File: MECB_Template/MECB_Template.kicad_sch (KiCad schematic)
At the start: 6 parts, among them J1 MECB_64AC, U1 ATF16V8

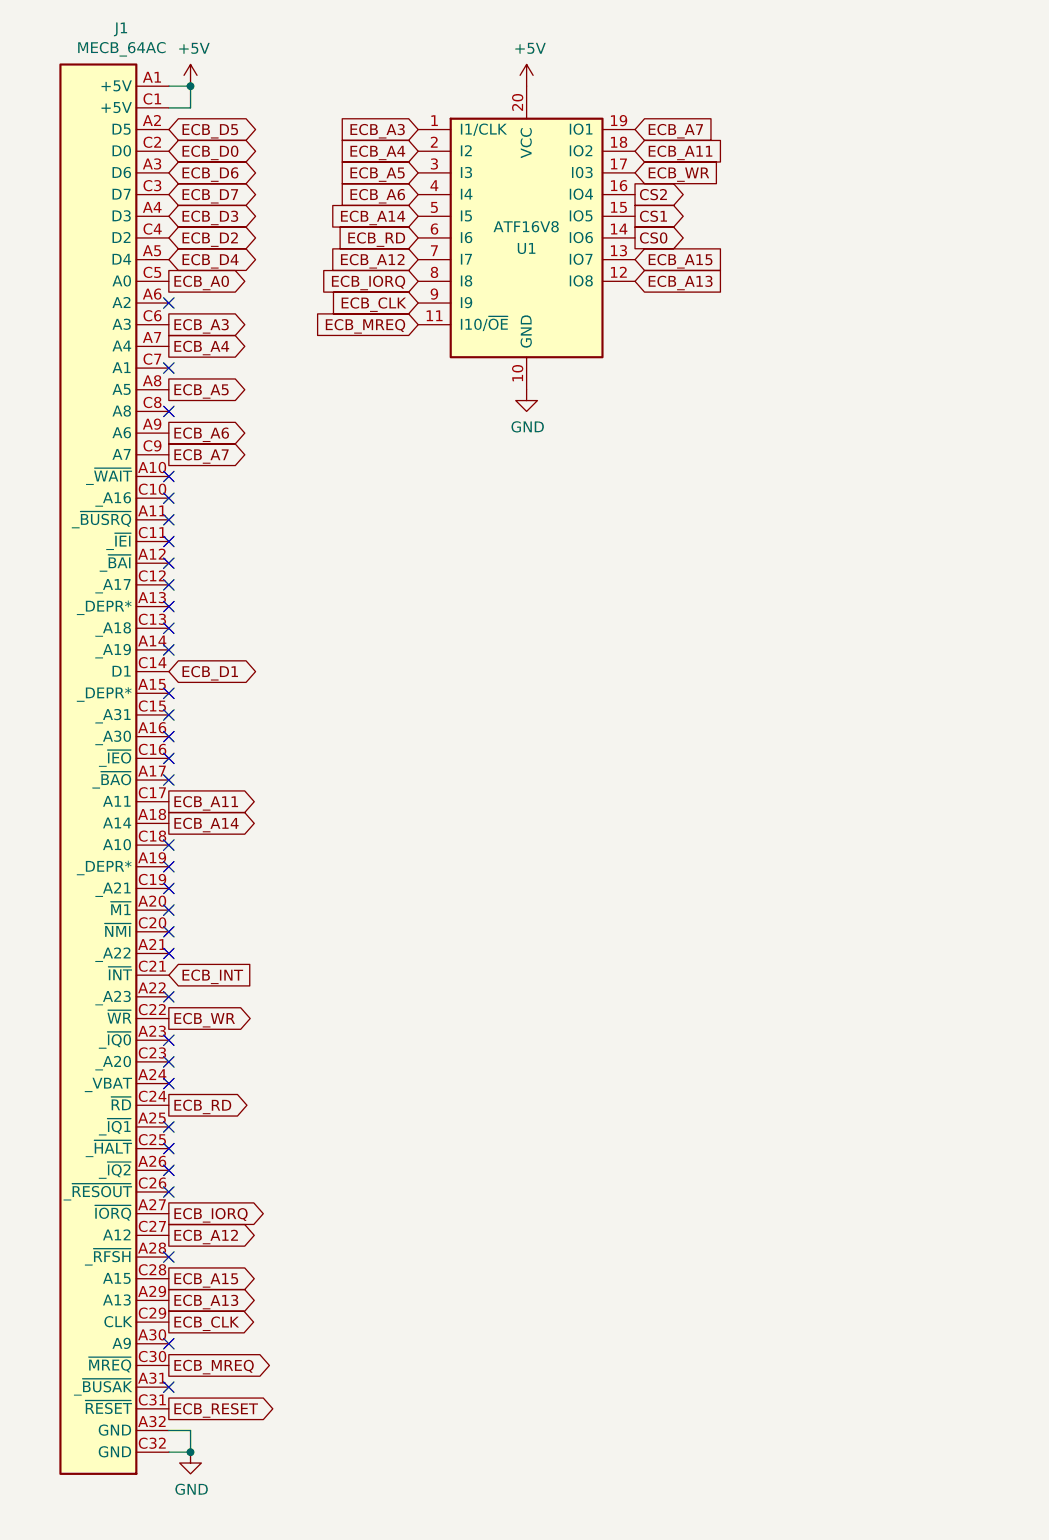
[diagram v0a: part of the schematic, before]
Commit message: Update MECB_Template files to KiCAD v7
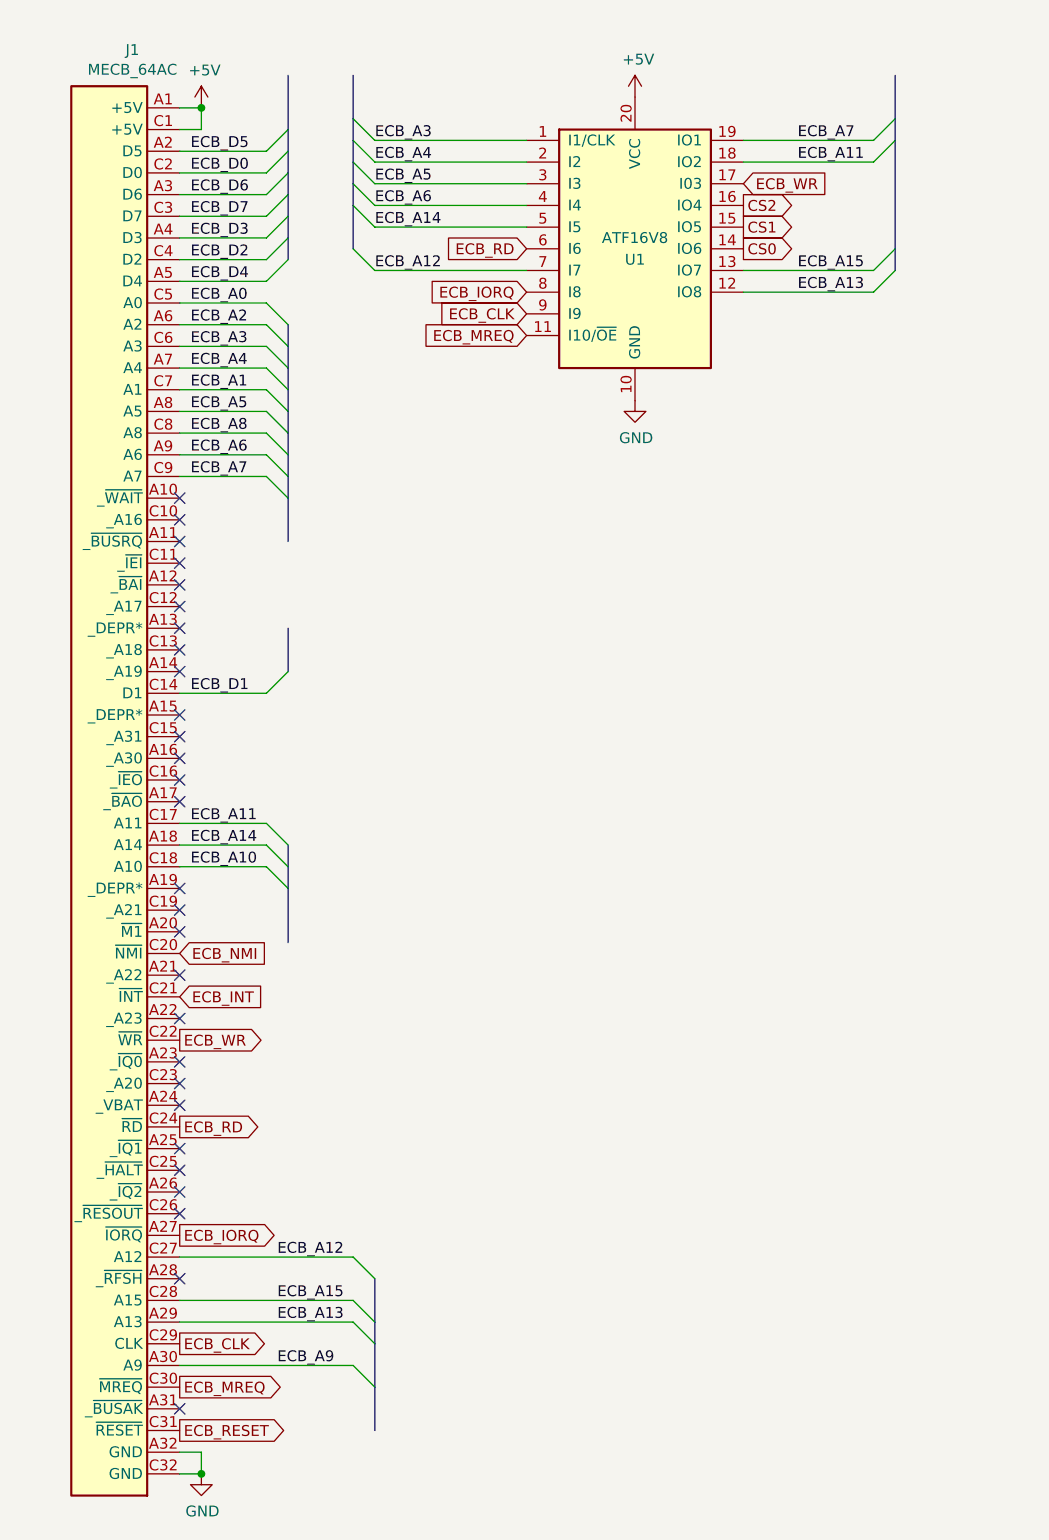
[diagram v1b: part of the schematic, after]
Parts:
- removed J1: MECB_64AC, MECB:DIN41612_C_2x32_C64AC_Male_Horizontal_THT, symbol MECB:MECB_64AC
- added J1: MECB_64AC, MyCustomFootprintLibrary:DIN41612_C_2x32_C64AC_Male_Horizontal_THT, symbol MyCustomSymbolLibrary:MECB_64AC
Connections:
- net +5V: now also J1.A1 (+5V), J1.C1 (+5V)
- net ECB_A0: now also J1.C5 (A0)
- net ECB_A11: now also J1.C17 (A11)
- net ECB_A12: now also J1.C27 (A12)
- net ECB_A13: now also J1.A29 (A13)
- net ECB_A14: now also J1.A18 (A14)
- net ECB_A15: now also J1.C28 (A15)
- net ECB_A3: now also J1.C6 (A3)
- net ECB_A4: now also J1.A7 (A4)
- net ECB_A5: now also J1.A8 (A5)
- net ECB_A6: now also J1.A9 (A6)
- net ECB_A7: now also J1.C9 (A7)
- net ECB_CLK: now also J1.C29 (CLK)
- net ECB_D0: now also J1.C2 (D0)
- net ECB_D1: now also J1.C14 (D1)
- net ECB_D2: now also J1.C4 (D2)
- net ECB_D3: now also J1.A4 (D3)
- net ECB_D4: now also J1.A5 (D4)
- net ECB_D5: now also J1.A2 (D5)
- net ECB_D6: now also J1.A3 (D6)
- net ECB_D7: now also J1.C3 (D7)
- net ECB_INT: now also J1.C21 (~{INT})
- net ECB_IORQ: now also J1.A27 (~{IORQ})
- net ECB_MREQ: now also J1.C30 (~{MREQ})
- net ECB_RD: now also J1.C24 (~{RD})
- net ECB_RESET: now also J1.C31 (~{RESET})
- net ECB_WR: now also J1.C22 (~{WR})
- net GND: now also J1.A32 (GND), J1.C32 (GND)
- new net ECB_A1: J1.C7 (A1)
- new net ECB_A10: J1.C18 (A10)
- new net ECB_A2: J1.A6 (A2)
- new net ECB_A8: J1.C8 (A8)
- new net ECB_A9: J1.A30 (A9)
- new net ECB_NMI: J1.C20 (~{NMI})
- no-connect marks 34 -> 28
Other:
- moved on the sheet: U1
